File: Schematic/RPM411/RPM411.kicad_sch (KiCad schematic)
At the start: 88 parts, among them J1 02x08_tbd, P1 P_Cap, Q1 tbd (GDS), U1 STM32F100C8Tb8, U2 TS5A9411, U3 TS5A9411, U4 TS5A9411, U5 74LVC3G04, U6 74LVC1G32, U7 TLV70030DDC

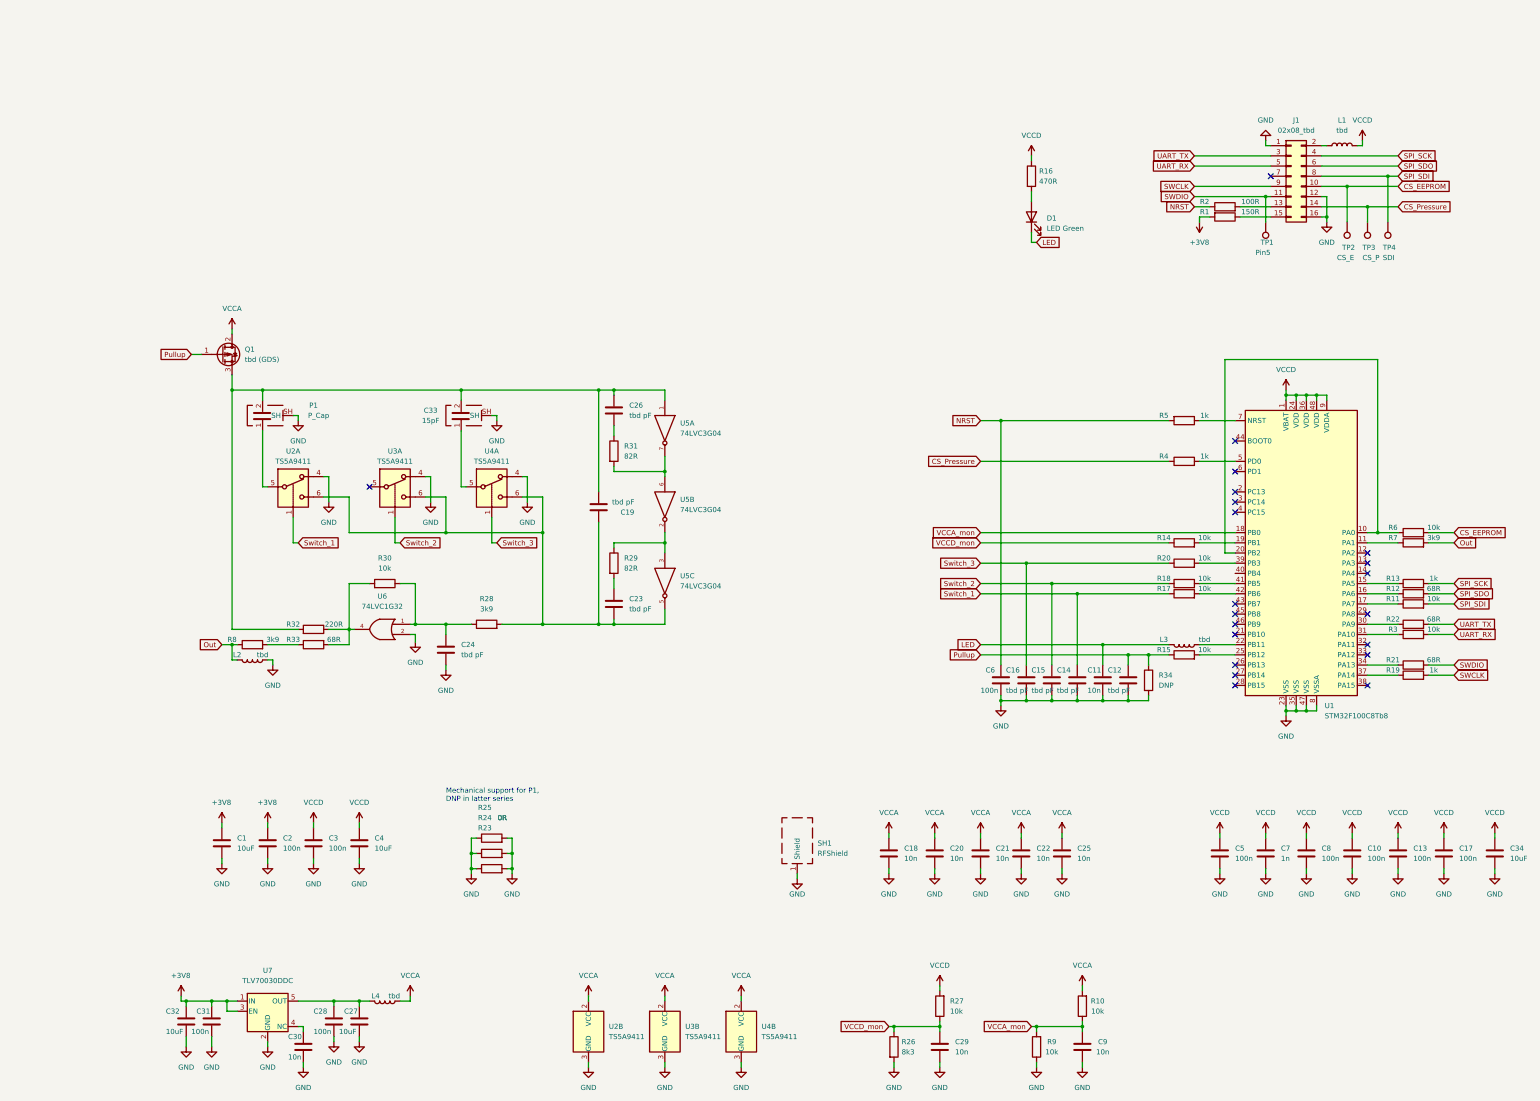
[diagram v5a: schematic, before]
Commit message: fixed erc errors
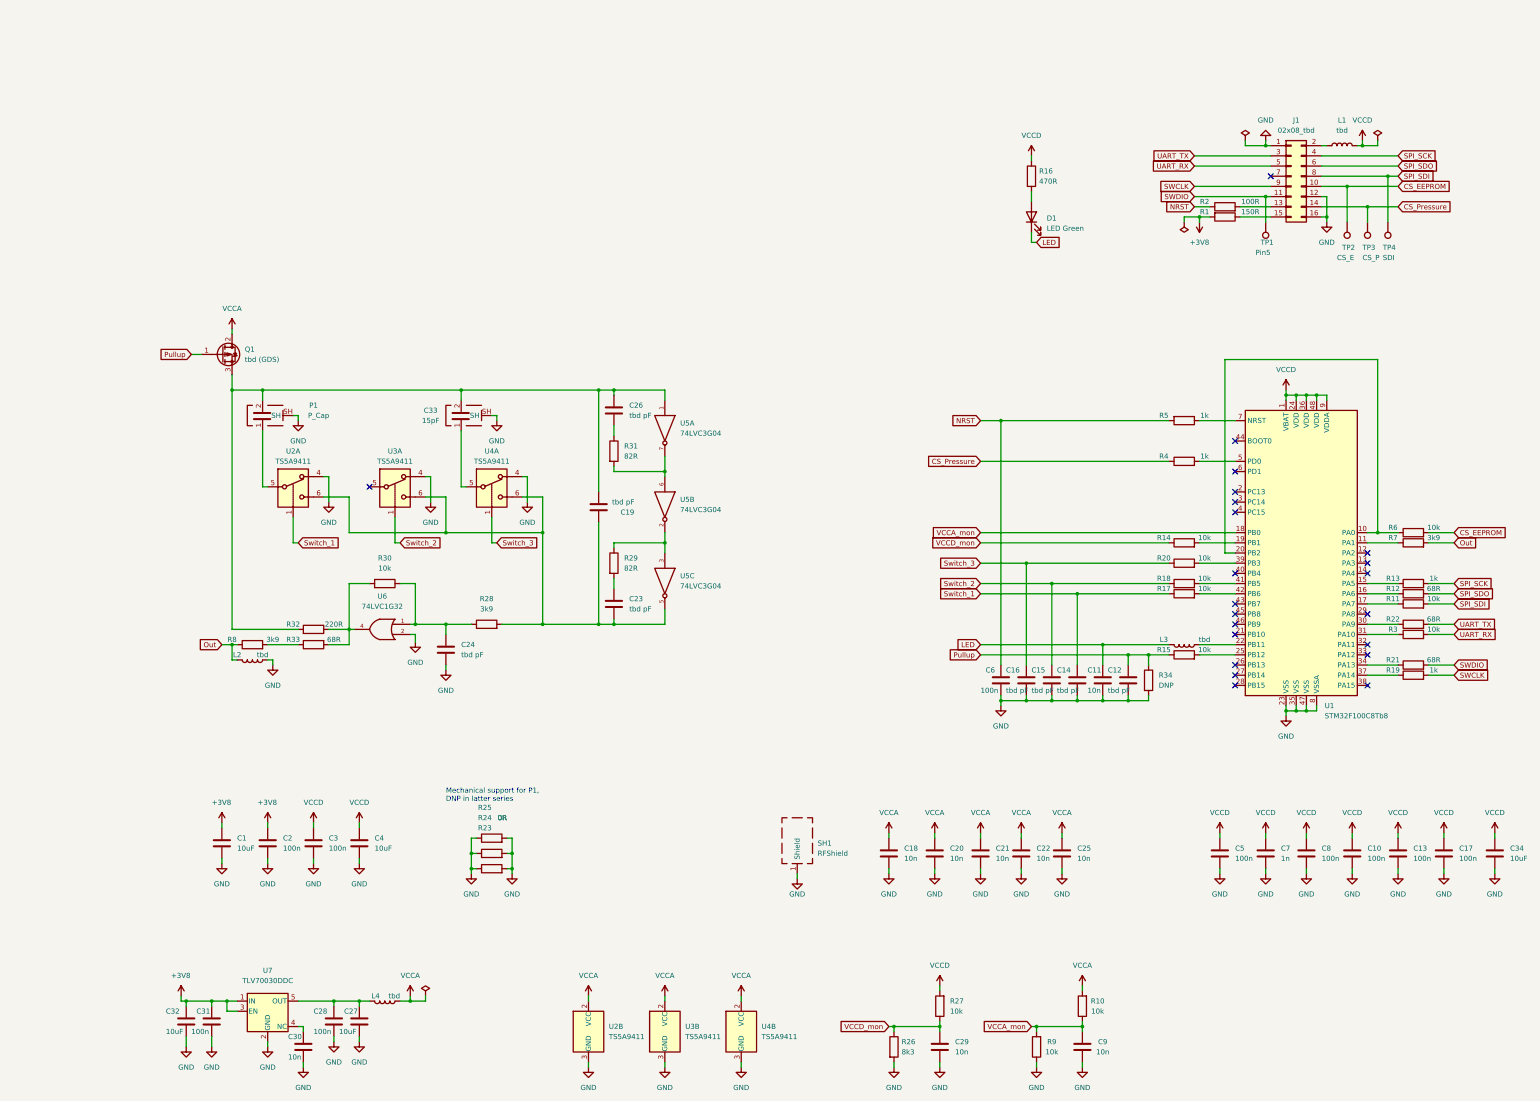
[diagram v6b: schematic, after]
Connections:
- net at U7.4 (NC): now also C30.1
- no-connect marks 21 -> 22
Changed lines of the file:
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@@
   (junction (at 260.35 179.07) (diameter 0) (color 0 0 0 0)
   )
+  (junction (at 326.39 40.64) (diameter 0) (color 0 0 0 0)
+  )
   (junction (at 128.27 220.98) (diameter 0) (color 0 0 0 0)
   )
   (junction (at 245.11 260.35) (diameter 0) (color 0 0 0 0)
   )
+  (junction (at 350.52 40.64) (diameter 0) (color 0 0 0 0)
+  )
   (junction (at 336.55 102.87) (diameter 0) (color 0 0 0 0)
   )
@@
   (junction (at 146.05 137.16) (diameter 0) (color 0 0 0 0)
   )
+  (junction (at 309.88 58.42) (diameter 0) (color 0 0 0 0)
+  )
   (junction (at 176.53 121.92) (diameter 0) (color 0 0 0 0)
   )
@@
   (junction (at 266.7 179.07) (diameter 0) (color 0 0 0 0)
   )
+  (junction (at 113.03 254) (diameter 0) (color 0 0 0 0)
+  )
   (junction (at 68.58 165.1) (diameter 0) (color 0 0 0 0)
   )
@@
   (no_connect (at 318.77 162.56))
   (no_connect (at 318.77 160.02))
-  (no_connect (at 351.79 165.1))
-  (no_connect (at 351.79 175.26))
   (no_connect (at 351.79 144.78))
   (no_connect (at 351.79 147.32))
-  (no_connect (at 351.79 142.24))
   (no_connect (at 351.79 167.64))
+  (no_connect (at 351.79 165.1))
+  (no_connect (at 351.79 175.26))
   (no_connect (at 102.87 125.73))
+  (no_connect (at 351.79 142.24))
   (no_connect (at 327.66 48.26))
+  (no_connect (at 318.77 147.32))
   (no_connect (at 351.79 157.48))
   (no_connect (at 318.77 121.92))
   (no_connect (at 318.77 157.48))
   (no_connect (at 318.77 154.94))
-  (no_connect (at 318.77 114.3))
   (no_connect (at 318.77 129.54))
   (no_connect (at 318.77 127))
   (no_connect (at 318.77 132.08))
+  (no_connect (at 318.77 114.3))
   (wire (pts (xy 285.75 177.8) (xy 285.75 179.07))
     (stroke (width 0) (type default) (color 0 0 0 0))
@@
     (stroke (width 0) (type default) (color 0 0 0 0))
   )
+  (wire (pts (xy 116.84 252.73) (xy 116.84 254))
+    (stroke (width 0) (type default) (color 0 0 0 0))
+  )
   (wire (pts (xy 69.85 256.54) (xy 67.31 256.54))
     (stroke (width 0) (type default) (color 0 0 0 0))
@@
     (stroke (width 0) (type default) (color 0 0 0 0))
   )
+  (wire (pts (xy 306.07 59.69) (xy 306.07 58.42))
+    (stroke (width 0) (type default) (color 0 0 0 0))
+  )
   (wire (pts (xy 93.98 262.89) (xy 93.98 264.16))
     (stroke (width 0) (type default) (color 0 0 0 0))
@@
     (stroke (width 0) (type default) (color 0 0 0 0))
   )
+  (wire (pts (xy 321.31 39.37) (xy 321.31 40.64))
+    (stroke (width 0) (type default) (color 0 0 0 0))
+  )
   (wire (pts (xy 273.05 149.86) (xy 302.26 149.86))
     (stroke (width 0) (type default) (color 0 0 0 0))
@@
     (stroke (width 0) (type default) (color 0 0 0 0))
   )
+  (wire (pts (xy 354.33 40.64) (xy 350.52 40.64))
+    (stroke (width 0) (type default) (color 0 0 0 0))
+  )
   (wire (pts (xy 233.68 269.24) (xy 233.68 270.51))
     (stroke (width 0) (type default) (color 0 0 0 0))
@@
     (stroke (width 0) (type default) (color 0 0 0 0))
   )
+  (wire (pts (xy 354.33 39.37) (xy 354.33 40.64))
+    (stroke (width 0) (type default) (color 0 0 0 0))
+  )
   (wire (pts (xy 383.54 220.98) (xy 383.54 222.25))
     (stroke (width 0) (type default) (color 0 0 0 0))
@@
     (stroke (width 0) (type default) (color 0 0 0 0))
   )
+  (wire (pts (xy 116.84 254) (xy 113.03 254))
+    (stroke (width 0) (type default) (color 0 0 0 0))
+  )
   (wire (pts (xy 266.7 177.8) (xy 266.7 179.07))
     (stroke (width 0) (type default) (color 0 0 0 0))
@@
     (stroke (width 0) (type default) (color 0 0 0 0))
   )
+  (wire (pts (xy 306.07 58.42) (xy 309.88 58.42))
+    (stroke (width 0) (type default) (color 0 0 0 0))
+  )
   (wire (pts (xy 128.27 220.98) (xy 129.54 220.98))
     (stroke (width 0) (type default) (color 0 0 0 0))
@@
     (stroke (width 0) (type default) (color 0 0 0 0))
   )
+  (wire (pts (xy 321.31 40.64) (xy 326.39 40.64))
+    (stroke (width 0) (type default) (color 0 0 0 0))
+  )
   (wire (pts (xy 279.4 177.8) (xy 279.4 179.07))
     (stroke (width 0) (type default) (color 0 0 0 0))
@@
     (pin "2")
   )
+  (symbol (lib_id "power:PWR_FLAG") (at 306.07 59.69 180) (unit 1)
+    (in_bom yes) (on_board yes) (fields_autoplaced)
+    (property "Reference" "#FLG0101" (id 0) (at 306.07 61.595 0)
+      (effects (font (size 1.27 1.27)) hide)
+    )
+    (property "Value" "PWR_FLAG" (id 1) (at 306.07 64.77 0)
+      (effects (font (size 1.27 1.27)) hide)
+    )
+    (property "Footprint" "" (id 2) (at 306.07 59.69 0)
+      (effects (font (size 1.27 1.27)) hide)
+    )
+    (property "Datasheet" "~" (id 3) (at 306.07 59.69 0)
+      (effects (font (size 1.27 1.27)) hide)
+    )
+    (pin "1")
+  )
   (symbol (lib_id "power:GND") (at 265.43 222.25 0) (unit 1)
     (in_bom yes) (on_board yes) (fields_autoplaced)
@@
     (pin "1")
   )
+  (symbol (lib_id "power:PWR_FLAG") (at 321.31 39.37 0) (unit 1)
+    (in_bom yes) (on_board yes) (fields_autoplaced)
+    (property "Reference" "#FLG0103" (id 0) (at 321.31 37.465 0)
+      (effects (font (size 1.27 1.27)) hide)
+    )
+    (property "Value" "PWR_FLAG" (id 1) (at 321.31 34.29 0)
+      (effects (font (size 1.27 1.27)) hide)
+    )
+    (property "Footprint" "" (id 2) (at 321.31 39.37 0)
+      (effects (font (size 1.27 1.27)) hide)
+    )
+    (property "Datasheet" "~" (id 3) (at 321.31 39.37 0)
+      (effects (font (size 1.27 1.27)) hide)
+    )
+    (pin "1")
+  )
   (symbol (lib_id "Device:R") (at 306.07 139.7 90) (unit 1)
     (in_bom yes) (on_board yes)
@@
     (pin "2")
   )
+  (symbol (lib_id "power:PWR_FLAG") (at 354.33 39.37 0) (unit 1)
+    (in_bom yes) (on_board yes) (fields_autoplaced)
+    (property "Reference" "#FLG0102" (id 0) (at 354.33 37.465 0)
+      (effects (font (size 1.27 1.27)) hide)
+    )
+    (property "Value" "PWR_FLAG" (id 1) (at 354.33 34.29 0)
+      (effects (font (size 1.27 1.27)) hide)
+    )
+    (property "Footprint" "" (id 2) (at 354.33 39.37 0)
+      (effects (font (size 1.27 1.27)) hide)
+    )
+    (property "Datasheet" "~" (id 3) (at 354.33 39.37 0)
+      (effects (font (size 1.27 1.27)) hide)
+    )
+    (pin "1")
+  )
   (symbol (lib_id "Device:R") (at 133.35 220.98 90) (unit 1)
     (in_bom yes) (on_board yes)
@@
     (pin "2")
   )
+  (symbol (lib_id "power:PWR_FLAG") (at 116.84 252.73 0) (unit 1)
+    (in_bom yes) (on_board yes) (fields_autoplaced)
+    (property "Reference" "#FLG0104" (id 0) (at 116.84 250.825 0)
+      (effects (font (size 1.27 1.27)) hide)
+    )
+    (property "Value" "PWR_FLAG" (id 1) (at 116.84 247.65 0)
+      (effects (font (size 1.27 1.27)) hide)
+    )
+    (property "Footprint" "" (id 2) (at 116.84 252.73 0)
+      (effects (font (size 1.27 1.27)) hide)
+    )
+    (property "Datasheet" "~" (id 3) (at 116.84 252.73 0)
+      (effects (font (size 1.27 1.27)) hide)
+    )
+    (pin "1")
+  )
   (symbol (lib_id "Device:C") (at 121.92 166.37 0) (unit 1)
     (in_bom yes) (on_board yes) (fields_autoplaced)
@@
   )
   (symbol_instances
+    (path "/234c2ece-8324-480d-a934-3683f8086a91"
+      (reference "#FLG0101") (unit 1) (value "PWR_FLAG") (footprint "")
+    )
+    (path "/7d2f7ba2-de8f-41db-a7d7-0f62b48a4a05"
+      (reference "#FLG0102") (unit 1) (value "PWR_FLAG") (footprint "")
+    )
+    (path "/759b2744-2cc2-41d9-b8cd-97014aacce51"
+      (reference "#FLG0103") (unit 1) (value "PWR_FLAG") (footprint "")
+    )
+    (path "/92c63725-c565-43ef-abbe-778a21ff274a"
+      (reference "#FLG0104") (unit 1) (value "PWR_FLAG") (footprint "")
+    )
     (path "/043a8473-47bd-4cf3-98c8-d8a9f87acbd8"
       (reference "#PWR01") (unit 1) (value "GND") (footprint "")

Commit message: sorted schematic
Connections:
- net at U7.4 (NC): now also C30.1
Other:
- company: (none) -> TjarkG
- title: (none) -> RPM411 Pressure Sensor
- moved on the sheet: C1, C10, C11, C12, C13, C14, C15, C16, C17, C18, C19, C2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
